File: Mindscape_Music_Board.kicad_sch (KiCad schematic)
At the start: 32 parts, among them J1 ISA, J2 AudioJack2, SW1 SW_DIP_x08, U1 74LS08, U2 74LS74, U3 LM386, U4 74LS04, U5 74LS08, U6 74LS85, U7 74LS85, U8 AY-3-8913, U9 AY-3-8913

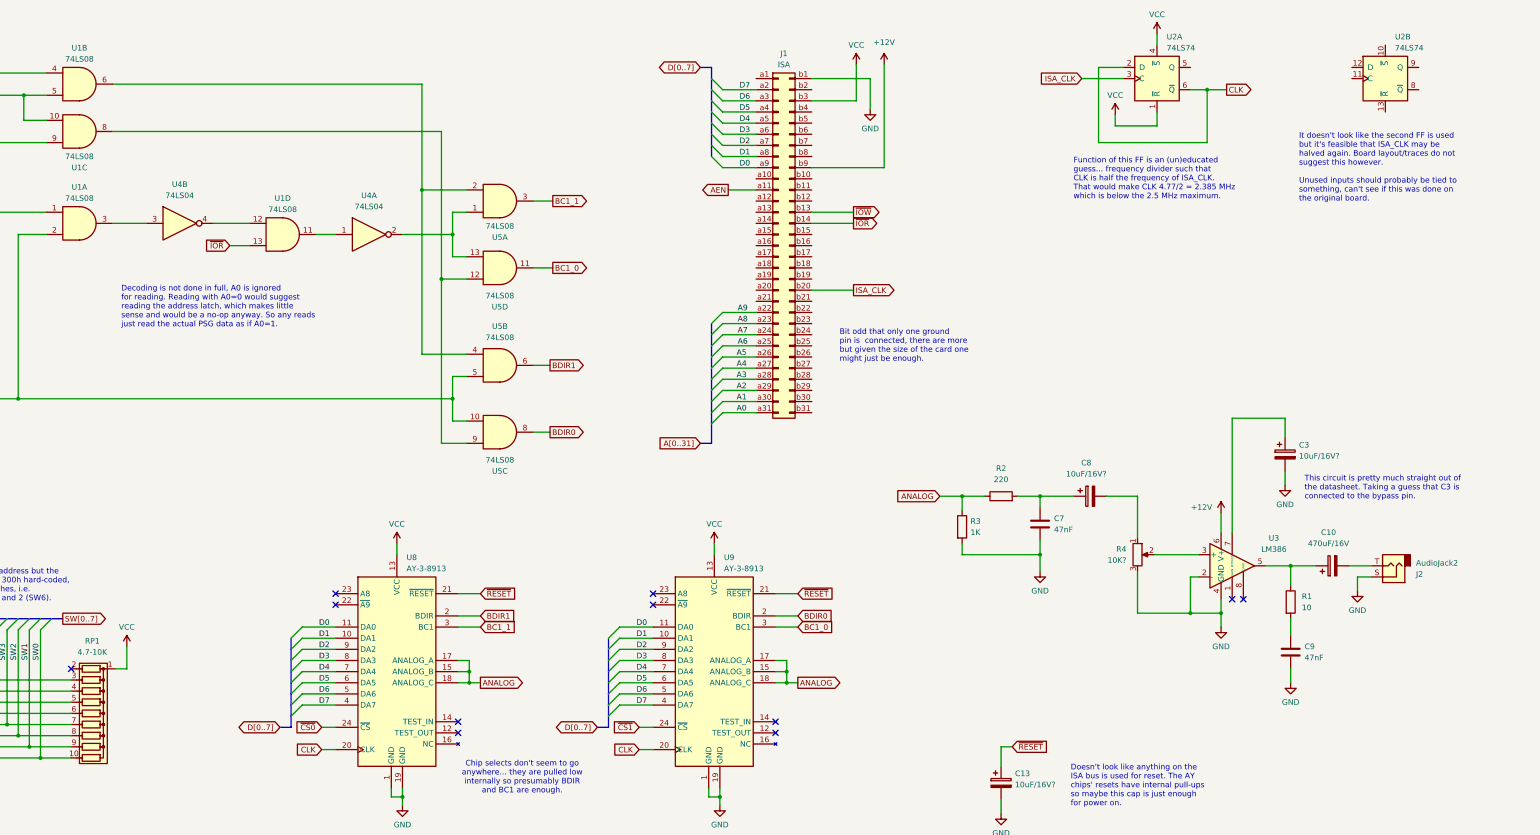
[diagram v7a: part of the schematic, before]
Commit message: Jumper to divide clock 1/2 or 1/4 speed.
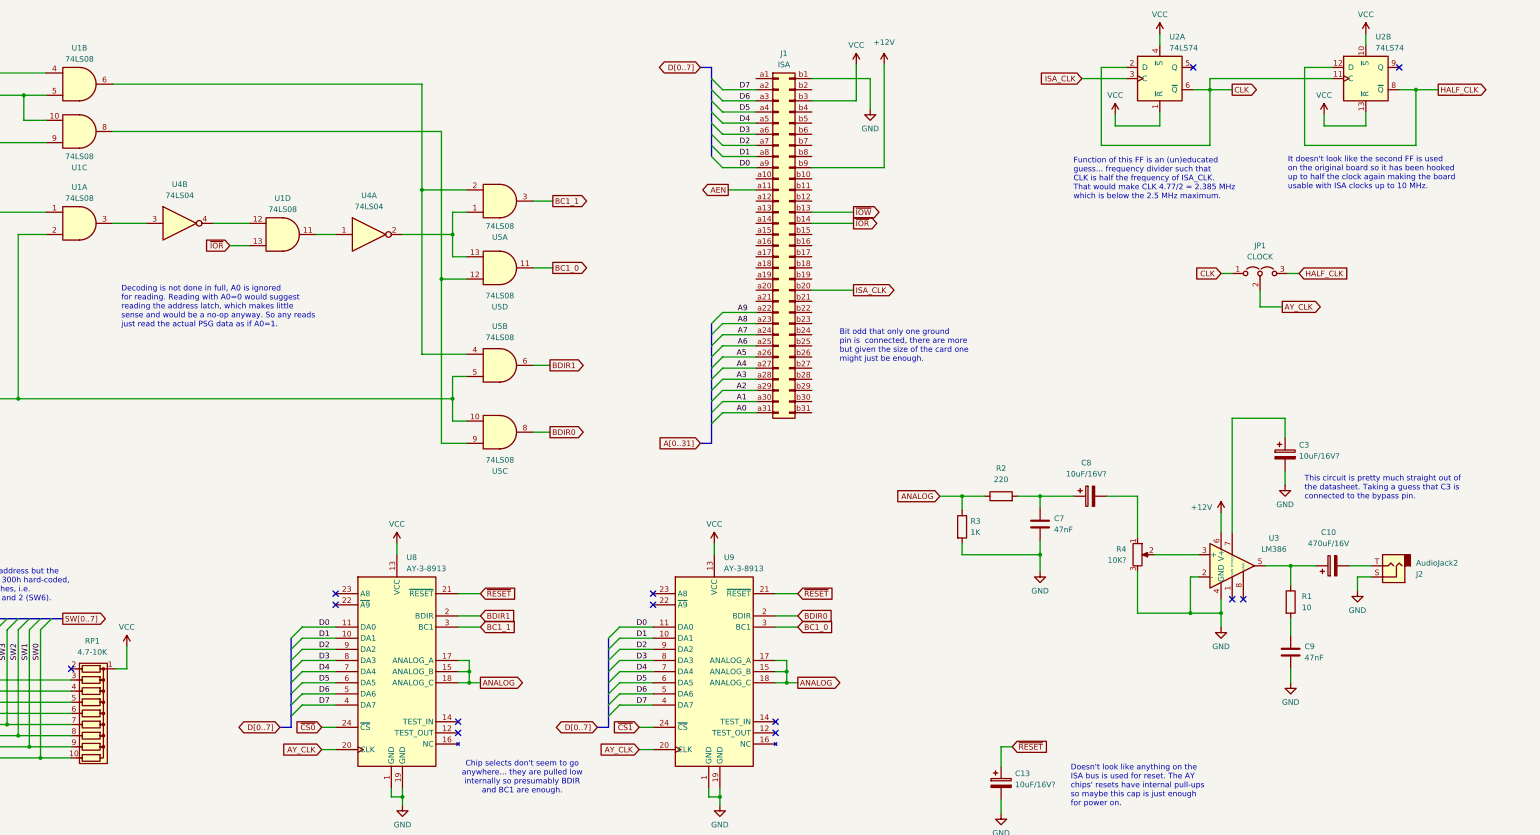
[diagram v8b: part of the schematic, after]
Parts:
- added JP1: CLOCK, Jumper:SolderJumper-3_P1.3mm_Open_RoundedPad1.0x1.5mm_NumberLabels, symbol Jumper:Jumper_3_Open
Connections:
- net CLK: now also U2.11 (C), JP1.1 (A); no longer U8.20 (CLK), U9.20 (CLK)
- net VCC: now also U2.10 (~{S}), U2.13 (~{R})
- net HALF_CLK: now reaches U2.12 (D)
- net HALF_CLK: now also U2.8 (~{Q}), JP1.3 (B)
- new net AY_CLK: JP1.2 (C), U8.20 (CLK), U9.20 (CLK)
- no-connect marks 13 -> 15
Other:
- note added: "It doesn't look like the second FF is used on the original board so it has been hooked up to half the clock again making the board usable with ISA clocks up to 10 MHz."
- note removed: "It doesn't look like the second FF is used but it's feasible that ISA_CLK may be halved again. Board layout/traces do not suggest this however. Unused inputs should probably be tied to something, can't see if this was done on the original board."
- moved on the sheet: U2A, U2B
